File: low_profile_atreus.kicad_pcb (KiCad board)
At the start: 2 copper layers, 232 x 90 mm, 140 parts, among them J1 Conn_02x03_Odd_Even, J3 USB_C_Receptacle, SW1 SW_Push, SW10 SW_Push, SW11 SW_Push, SW12 SW_Push, SW13 SW_Push, SW14 SW_Push, SW15 SW_Push, SW16 SW_Push, SW17 SW_Push, SW18 SW_Push, SW19 SW_Push, SW2 SW_Push, SW20 SW_Push, SW21 SW_Push, SW22 SW_Push, SW23 SW_Push, SW24 SW_Push, SW25 SW_Push, SW26 SW_Push, SW27 SW_Push, SW28 SW_Push, SW29 SW_Push, SW3 SW_Push, SW30 SW_Push, SW31 SW_Push, SW32 SW_Push, SW33 SW_Push, SW34 SW_Push, SW35 SW_Push, SW36 SW_Push, SW37 SW_Push, SW38 SW_Push, SW39 SW_Push, SW4 SW_Push, SW40 SW_Push, SW41 SW_Push, SW42 SW_Push, SW5 SW_Push, SW6 SW_Push, SW7 SW_Push, SW8 SW_Push, SW9 SW_Push, U3 ATmega32U4-A, Y1 Crystal

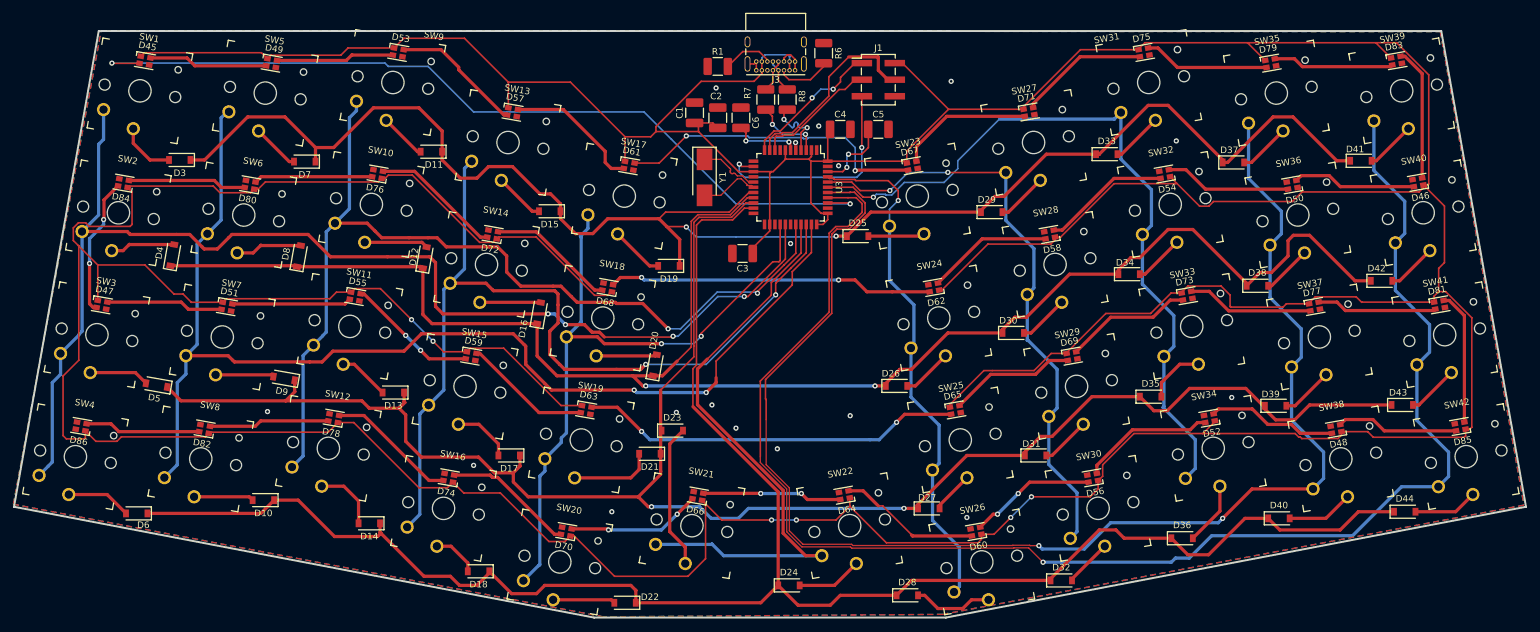
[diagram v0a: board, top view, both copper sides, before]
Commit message: Atreus Low Profile PCB Version 1.0.0
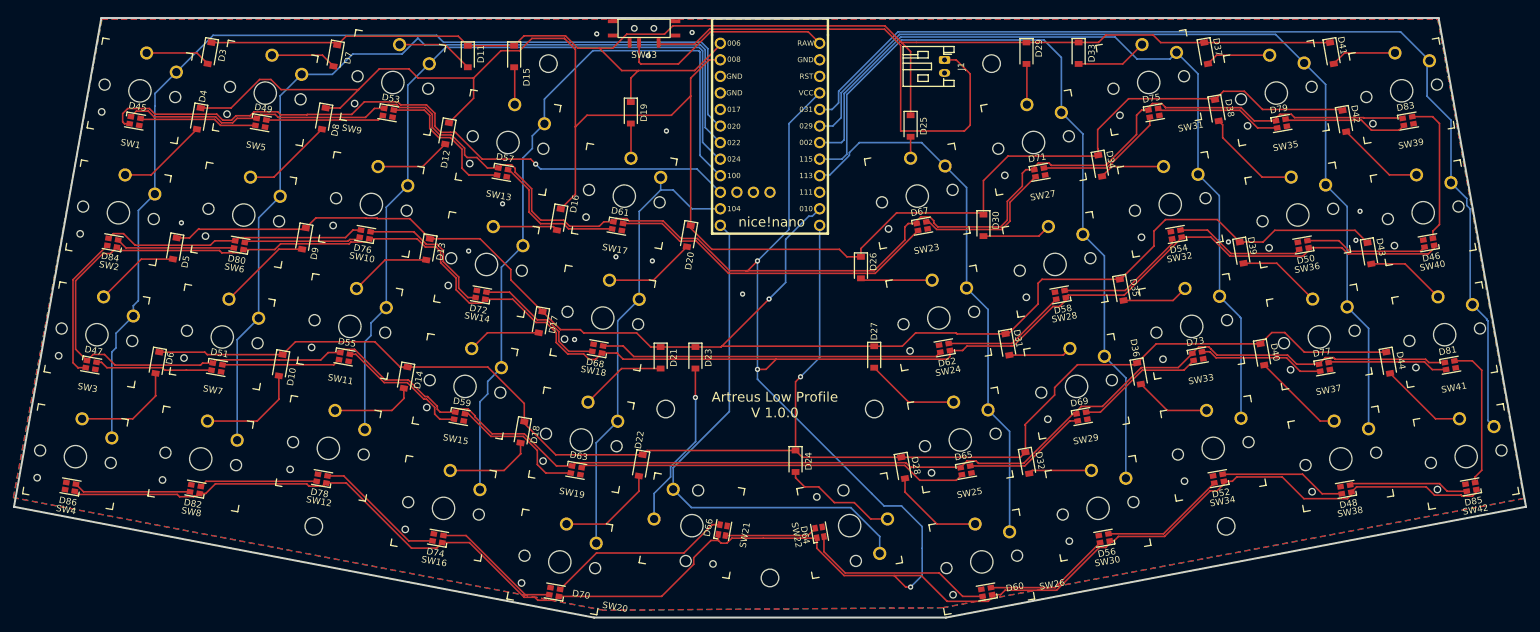
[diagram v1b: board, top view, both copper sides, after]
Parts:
- removed C1: 10 uF, Capacitor_SMD:C_1210_3225Metric_Pad1.33x2.70mm_HandSolder
- removed C2, C3, C4: 100 nF, Capacitor_SMD:C_1210_3225Metric_Pad1.33x2.70mm_HandSolder
- removed C5, C6: 1 uF, Capacitor_SMD:C_1210_3225Metric_Pad1.33x2.70mm_HandSolder
- removed J3: USB_C_Receptacle, Connector_USB:USB_C_Receptacle_GCT_USB4085
- removed R1, R6: 5.1 k, Resistor_SMD:R_1210_3225Metric_Pad1.30x2.65mm_HandSolder
- removed R7, R8: 22 +- 5 %, Resistor_SMD:R_1210_3225Metric_Pad1.30x2.65mm_HandSolder
- removed U3: ATmega32U4-A, Package_QFP:TQFP-44_10x10mm_P0.8mm
- removed Y1: Crystal, Crystal:Crystal_SMD_Abracon_ABM3-2Pin_5.0x3.2mm_HandSoldering
- added Mounting Hole 2: MountingHole_2.7mm_M2.5, MountingHole:MountingHole_2.7mm_M2.5, F.Cu at (134.0, 105.9)
- added Mounting Hole 3: MountingHole_2.7mm_M2.5, MountingHole:MountingHole_2.7mm_M2.5, F.Cu at (204.0, 98.0)
- added Mounting Hole 4: MountingHole_2.7mm_M2.5, MountingHole:MountingHole_2.7mm_M2.5, F.Cu at (100.0, 27.0)
- added Mounting Hole 5: MountingHole_2.7mm_M2.5, MountingHole:MountingHole_2.7mm_M2.5, F.Cu at (168.0, 27.0)
- added Mounting Hole 6: MountingHole_2.7mm_M2.5, MountingHole:MountingHole_2.7mm_M2.5, F.Cu at (118.0, 80.0)
- added Mounting Hole 7: MountingHole_2.7mm_M2.5, MountingHole:MountingHole_2.7mm_M2.5, F.Cu at (150.0, 80.0)
- added SW43: SW_SPDT, VoidSwitch:MSK12C02, F.Cu at (114.7, 21.6)
- added U1: nice_nano, nice-nano-kicad-master:nice_nano, F.Cu at (134.0, 37.8)
- added mounting Hole 1: MountingHole_2.7mm_M2.5, MountingHole:MountingHole_2.7mm_M2.5, F.Cu at (64.0, 98.0)
- J1: value Conn_02x03_Odd_Even -> Conn_01x02_Female; footprint Connector_PinHeader_2.54mm:PinHeader_2x03_P2.54mm_Vertical_SMD -> Connector_JST:JST_PH_S2B-PH-K_1x02_P2.00mm_Horizontal
- moved D38 27.6 mm to (202.6, 34.2), turned to -80 degrees
- moved D36 26.1 mm to (190.6, 74.5), turned to -80 degrees
- moved D40 25.3 mm to (209.6, 71.6), turned to -80 degrees
- moved D42 25.2 mm to (222.1, 35.8), turned to -80 degrees
- moved D29 25.0 mm to (173.4, 25.4), turned to -90 degrees
- moved D27 24.7 mm to (150.0, 72.0), turned to -90 degrees
- moved D15 24.4 mm to (94.7, 25.9), turned to -90 degrees
- moved D19 24.2 mm to (112.6, 34.5), turned to -90 degrees
- moved D39 24.1 mm to (206.4, 56.0), turned to -80 degrees
- moved D43 23.8 mm to (226.0, 56.1), turned to -80 degrees
- moved D6 23.3 mm to (40.0, 72.9), turned to -100 degrees
- moved D14 23.0 mm to (78.1, 75.2), turned to -100 degrees
- moved D44 23.0 mm to (228.9, 72.9), turned to -80 degrees
- moved D13 22.6 mm to (81.5, 55.5), turned to -100 degrees
- moved D18 22.4 mm to (96.0, 83.6), turned to -100 degrees
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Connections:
- D45 pad 1: VBUS -> +3V3
- D46 pad 1: VBUS -> +3V3
- D47 pad 1: VBUS -> +3V3
- D48 pad 1: VBUS -> +3V3
- D49 pad 1: VBUS -> +3V3
- D50 pad 1: VBUS -> +3V3
- D51 pad 1: VBUS -> +3V3
- D52 pad 1: VBUS -> +3V3
- D53 pad 1: VBUS -> +3V3
- D54 pad 1: VBUS -> +3V3
- D55 pad 1: VBUS -> +3V3
- D56 pad 1: VBUS -> +3V3
- D57 pad 1: VBUS -> +3V3
- D58 pad 1: VBUS -> +3V3
- D59 pad 1: VBUS -> +3V3
- D60 pad 1: VBUS -> +3V3
- D61 pad 1: VBUS -> +3V3
- D62 pad 1: VBUS -> +3V3
- D63 pad 1: VBUS -> +3V3
- D64 pad 1: VBUS -> +3V3
- D65 pad 1: VBUS -> +3V3
- D66 pad 1: VBUS -> +3V3
- D67 pad 1: VBUS -> +3V3
- D68 pad 1: VBUS -> +3V3
- D69 pad 1: VBUS -> +3V3
- D70 pad 1: VBUS -> +3V3
- D71 pad 1: VBUS -> +3V3
- D72 pad 1: VBUS -> +3V3
- D73 pad 1: VBUS -> +3V3
- D74 pad 1: VBUS -> +3V3
- D75 pad 1: VBUS -> +3V3
- D76 pad 1: VBUS -> +3V3
- D77 pad 1: VBUS -> +3V3
- D78 pad 1: VBUS -> +3V3
- D79 pad 1: VBUS -> +3V3
- D80 pad 1: VBUS -> +3V3
- D81 pad 1: VBUS -> +3V3
- D82 pad 1: VBUS -> +3V3
- D83 pad 1: VBUS -> +3V3
- D84 pad 1: VBUS -> +3V3
- D85 pad 1: VBUS -> +3V3
- D86 pad 1: VBUS -> +3V3
- J1 pad 1: MISO -> Net-(J1-Pad1)
- J1 pad 2: VBUS -> GND
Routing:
- net +3V3: track 0.00 -> 1062.1 mm, vias 0 -> 3
- net VBUS: track 1039.9 -> 0.00 mm, vias 6 -> 0
- net Net-(J1-Pad1): track 0.00 -> 76.0 mm
- net COL10: track 236.4 -> 161.9 mm, vias 1 -> 0
- net COL9: track 215.3 -> 144.4 mm, vias 2 -> 0
- net ROW2: track 279.0 -> 235.2 mm, vias 2 -> 1
- net ROW3: track 288.6 -> 247.4 mm, vias 0 -> 1
- net COL1: track 180.3 -> 140.5 mm, vias 2 -> 0
- net RST: track 34.7 -> 0.00 mm, vias 2 -> 0
- net COL4: track 104.7 -> 70.6 mm, vias 2 -> 0
- net +BATT: track 0.00 -> 33.6 mm
- net GND: track 7.25 -> 40.7 mm, vias 17 -> 14
- net COL0: track 190.9 -> 157.8 mm, vias 4 -> 0
- net MOSI: track 30.5 -> 0.00 mm
- net COL3: track 140.4 -> 111.3 mm, vias 2 -> 0
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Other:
- board size 232 x 90 mm -> 232 x 92 mm
- board text added: "Artreus Low Profile V 1.0.0"
